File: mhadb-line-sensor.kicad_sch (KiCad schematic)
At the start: 11 parts, among them U1 STM32F103C8Tx

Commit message: schem: import HSE and boot/rst
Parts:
- added C11: 0u1, Capacitor_SMD:C_0402_1005Metric, symbol Device:C
- added C13, C14: 20p, Capacitor_SMD:C_0603_1608Metric, symbol Device:C
- added R18: 10k, Resistor_SMD:R_0402_1005Metric, symbol Device:R
- added R19: 560, Resistor_SMD:R_0603_1608Metric, symbol Device:R_Small
- added Y1: 8M, Crystal:Crystal_SMD_5032-2Pin_5.0x3.2mm, symbol Device:Crystal
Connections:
- net GND: now also C11.2, C13.2, C14.2, R18.1
- net BOOT: now reaches U1.44 (BOOT0)
- net BOOT: now also R18.2
- net XTAL_I: now reaches U1.5 (PD0)
- net XTAL_I: now also C13.1, Y1.2
- net XTAL_O: now reaches U1.6 (PD1)
- net XTAL_O: now also R19.2
- net NRST: now reaches U1.7 (NRST)
- net NRST: now also C11.1
- new net XTAL_RO: C14.1, R19.1, Y1.1
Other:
- note added: "HSE"

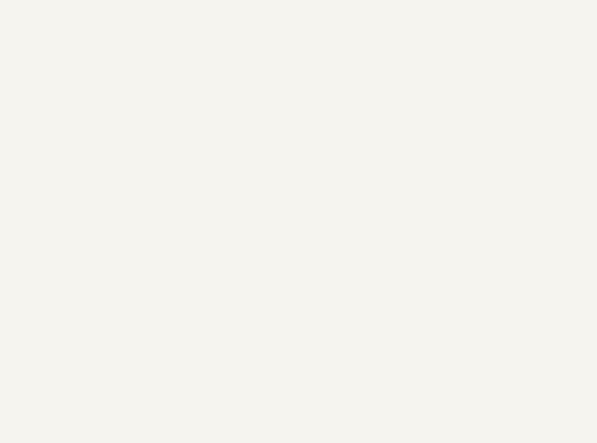
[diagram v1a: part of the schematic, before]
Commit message: schem: add CAN/Power connector
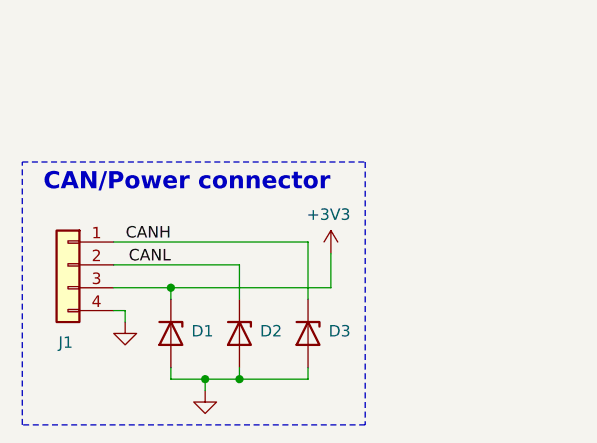
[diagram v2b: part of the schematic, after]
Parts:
- added D1, D2, D3: H5VU10U, Pers:Diode_DFN1006, symbol Pers:H5VU10U
- added J1: Conn_01x04, symbol Connector_Generic:Conn_01x04
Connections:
- net +3V3: now also D1.1 (K), J1.3 (Pin_3)
- net GND: now also D1.2 (A), D2.2 (A), D3.2 (A), J1.4 (Pin_4)
- new net CANH: D3.1 (K), J1.1 (Pin_1)
- new net CANL: D2.1 (K), J1.2 (Pin_2)
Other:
- note added: "CAN/Power connector"

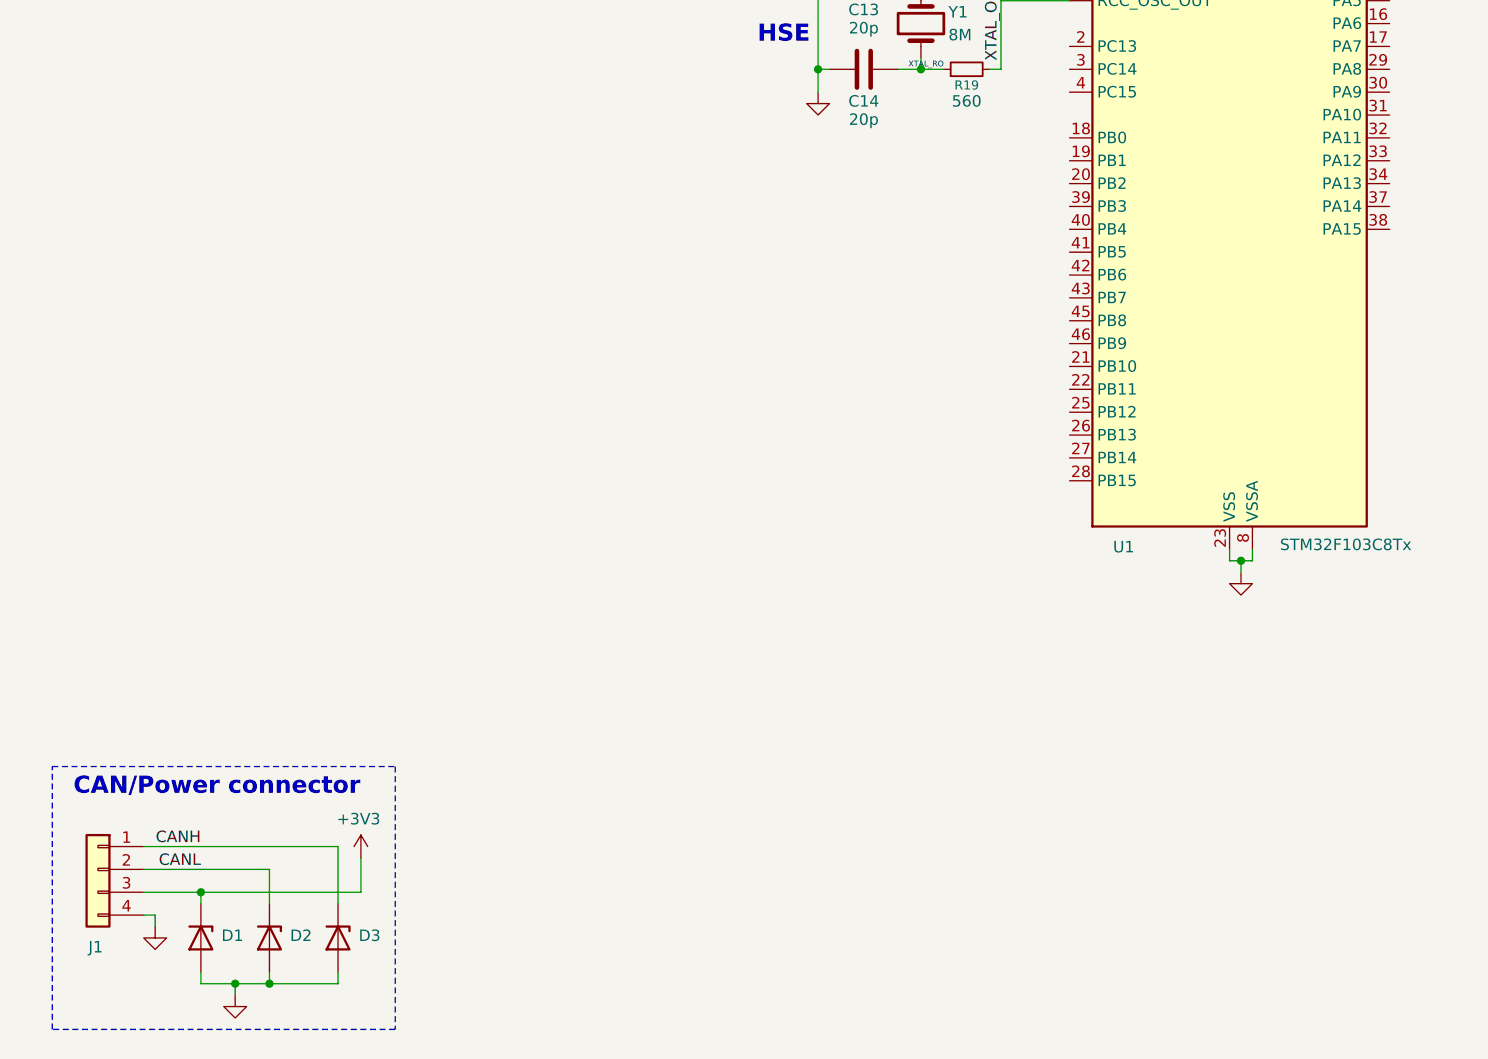
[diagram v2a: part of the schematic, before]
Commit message: schem: add TC2030 SWD debug port
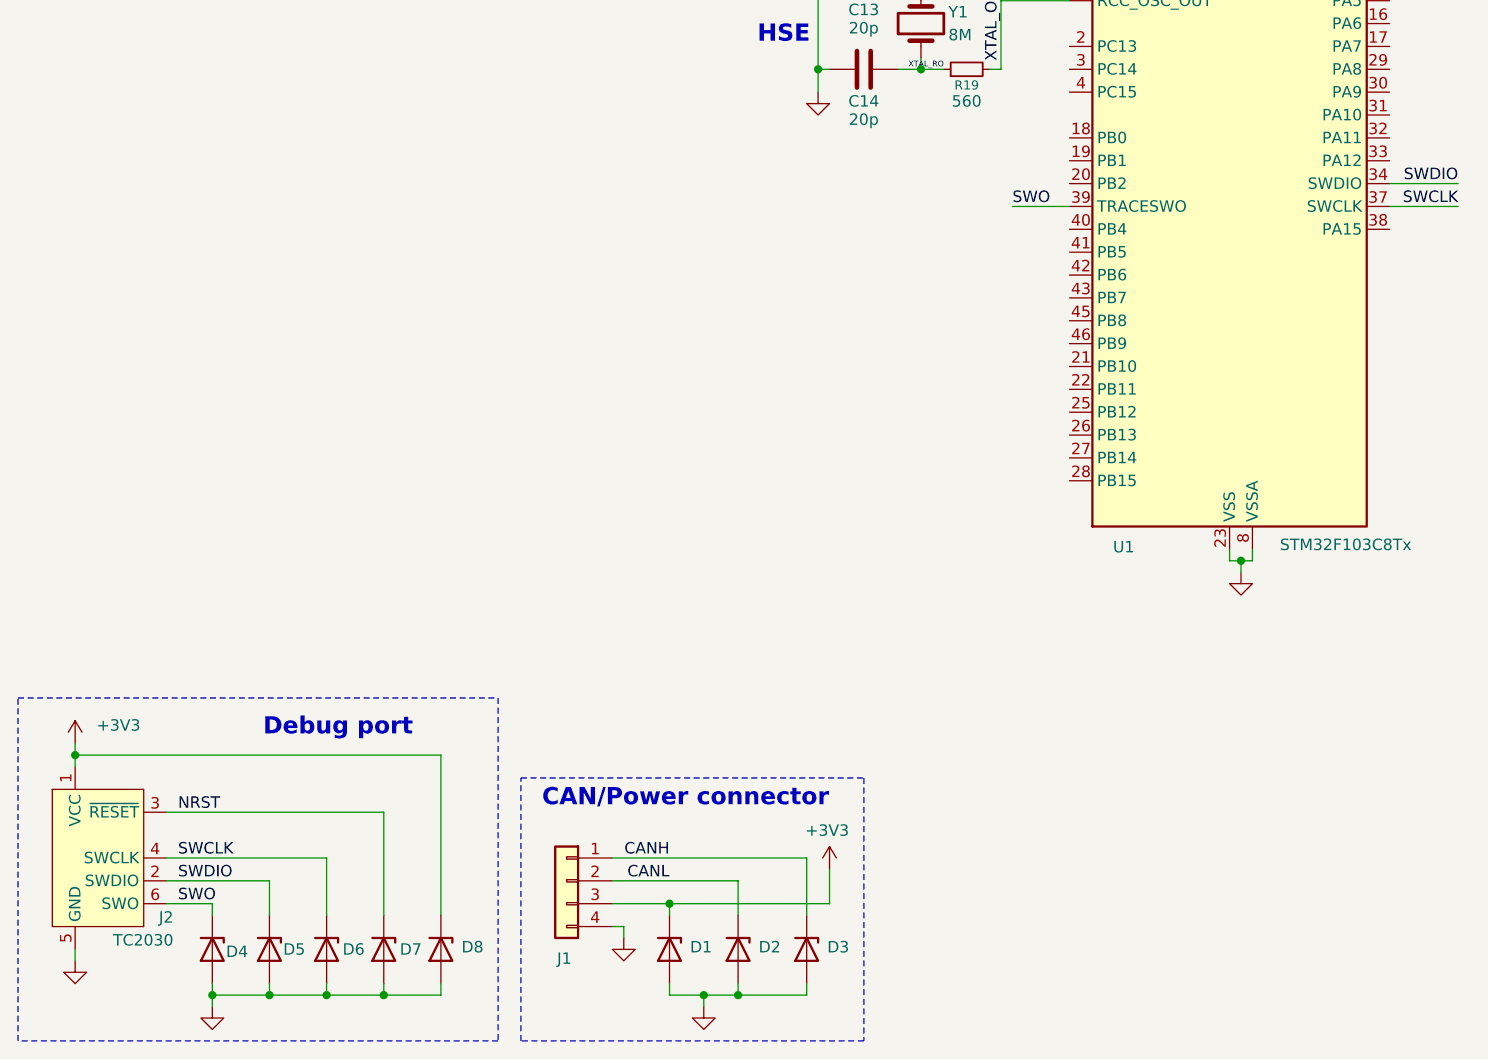
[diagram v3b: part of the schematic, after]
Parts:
- added D4, D5, D6, D7, D8: H5VU10U, Pers:Diode_DFN1006, symbol Pers:H5VU10U
- added J2: TC2030, Connector:Tag-Connect_TC2030-IDC-NL_2x03_P1.27mm_Vertical, symbol Connector:Conn_ARM_SWD_TagConnect_TC2030-NL
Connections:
- net +3V3: now also D8.1 (K), J2.1 (VCC)
- net GND: now also D4.2 (A), D5.2 (A), D6.2 (A), D7.2 (A), D8.2 (A), J2.5 (GND)
- net NRST: now also D7.1 (K), J2.3 (~{RESET})
- net SWDIO: now reaches U1.34 (PA13)
- net SWDIO: now also D5.1 (K), J2.2 (SWDIO)
- net SWCLK: now reaches U1.37 (PA14)
- net SWCLK: now also D6.1 (K), J2.4 (SWCLK)
- net SWO: now reaches U1.39 (PB3)
- net SWO: now also D4.1 (K), J2.6 (SWO)
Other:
- note added: "Debug port"
- moved on the sheet: D1, D2, D3, J1

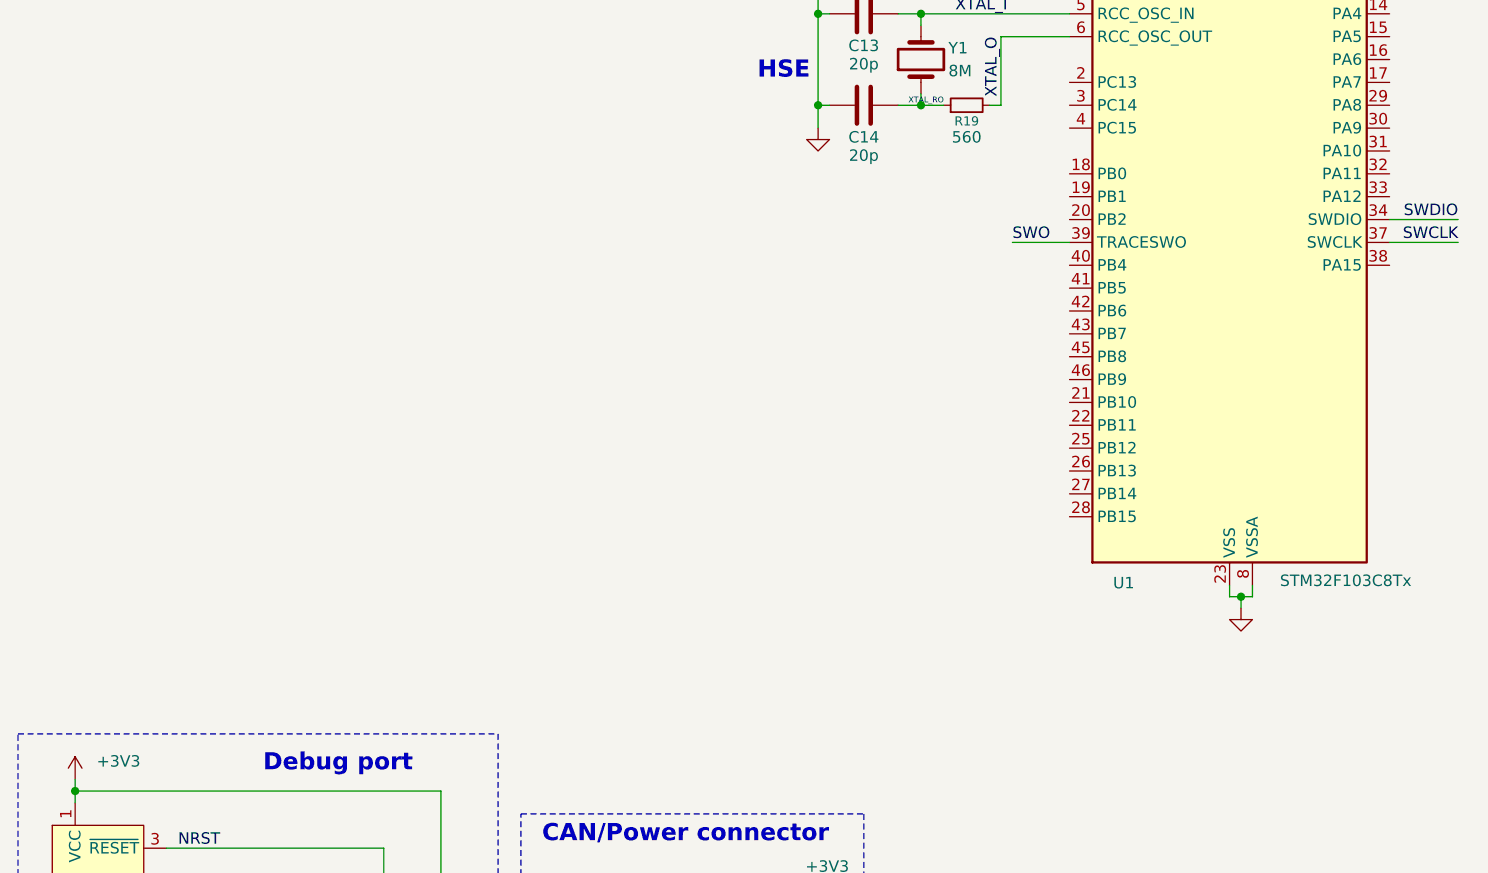
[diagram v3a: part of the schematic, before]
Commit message: schem: add SN65HVD230 CAN transceiver
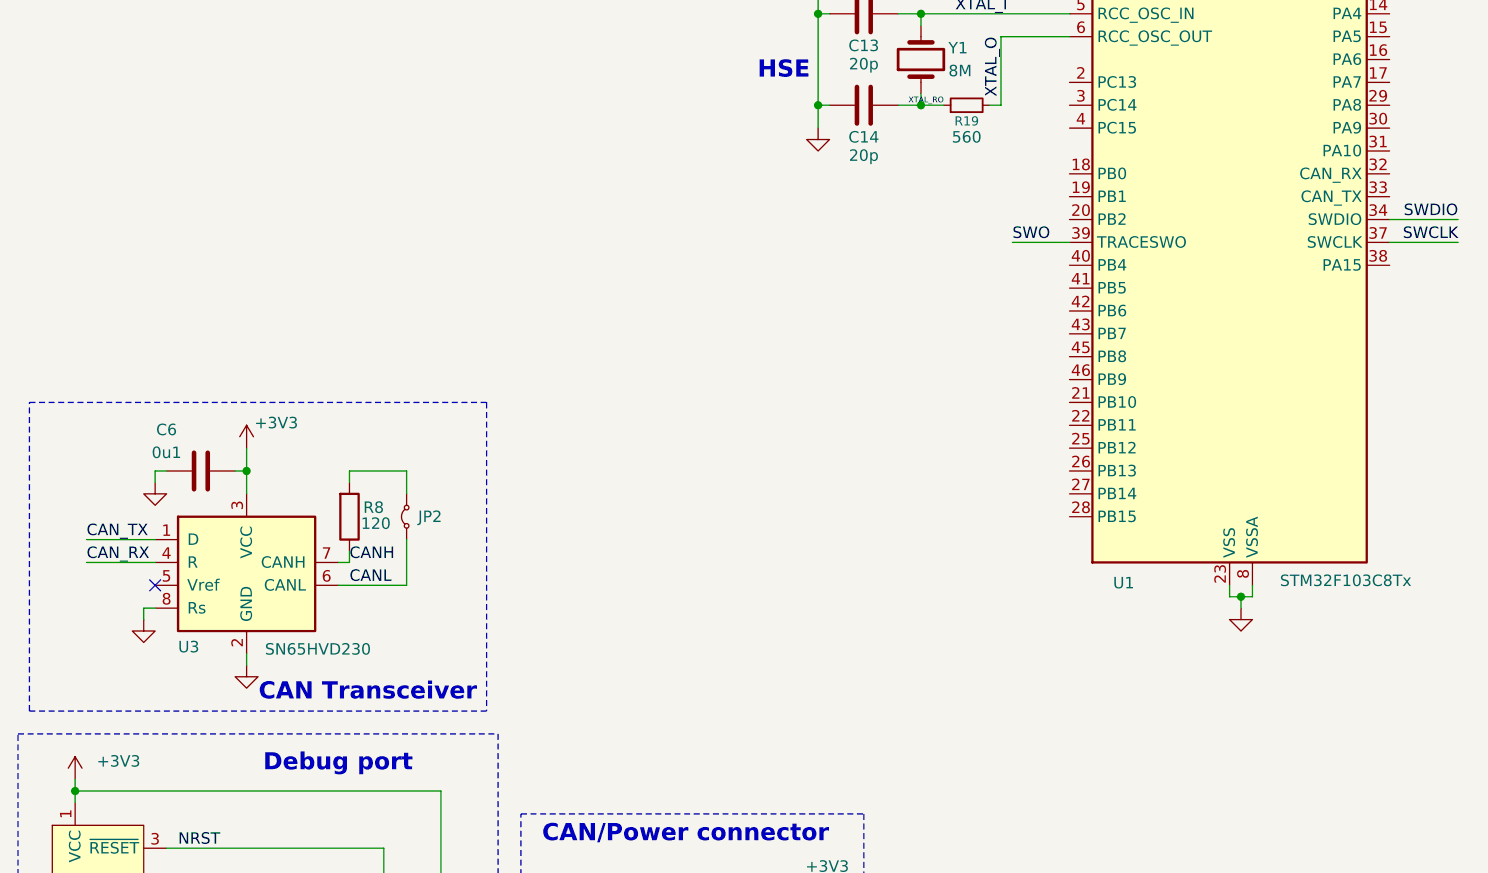
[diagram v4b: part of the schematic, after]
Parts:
- added C6: 0u1, Capacitor_SMD:C_0402_1005Metric, symbol Device:C
- added JP2: Jumper_2_Small_Bridged, Jumper:SolderJumper-2_P1.3mm_Open_RoundedPad1.0x1.5mm, symbol Jumper:Jumper_2_Small_Bridged
- added R8: 120, Resistor_SMD:R_1206_3216Metric, symbol Device:R
- added U3: SN65HVD230, Package_SO:SOIC-8_3.9x4.9mm_P1.27mm, symbol Interface_CAN_LIN:SN65HVD230
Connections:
- net +3V3: now also C6.1, U3.3 (VCC)
- net CANH: now also R8.1, U3.7 (CANH)
- net CANL: now also JP2.1 (A), U3.6 (CANL)
- net GND: now also C6.2, U3.2 (GND), U3.8 (Rs)
- new net: JP2.2 (B), R8.2
- new net CAN_RX: U3.4 (R)
- new net CAN_TX: U3.1 (D)
- no-connect marks 0 -> 1
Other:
- note added: "CAN Transceiver"

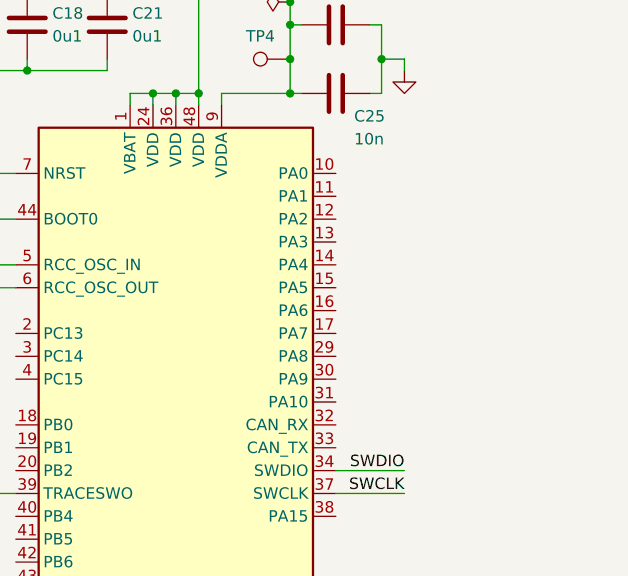
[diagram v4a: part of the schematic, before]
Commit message: schem: add UART1 header
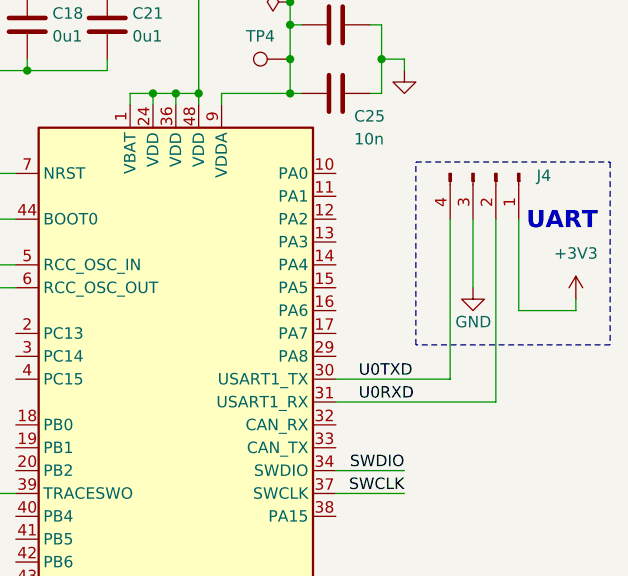
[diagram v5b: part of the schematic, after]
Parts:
- added J4: Conn_01x04_Pin, Connector_PinHeader_2.54mm:PinHeader_1x04_P2.54mm_Vertical, symbol Connector:Conn_01x04_Pin
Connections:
- net +3V3: now also J4.1 (Pin_1)
- net GND: now also J4.3 (Pin_3)
- net U0TXD: now reaches U1.30 (PA9)
- net U0TXD: now also J4.4 (Pin_4)
- net U0RXD: now reaches U1.31 (PA10)
- net U0RXD: now also J4.2 (Pin_2)
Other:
- note added: "UART"
